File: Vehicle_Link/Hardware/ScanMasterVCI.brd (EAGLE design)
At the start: 53 x 39.4 mm, 88 parts, among them IC1 XMEGA32A4U, Q1 MMBT4403, Q10 ZXMP6A17G, Q2 MMBT3904, Q3 MMBT3904, Q4 MMBT3904, Q5 MMBT3904, Q6 MMBT3904, Q7 NTZD5110N, Q8 NTZD5110N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

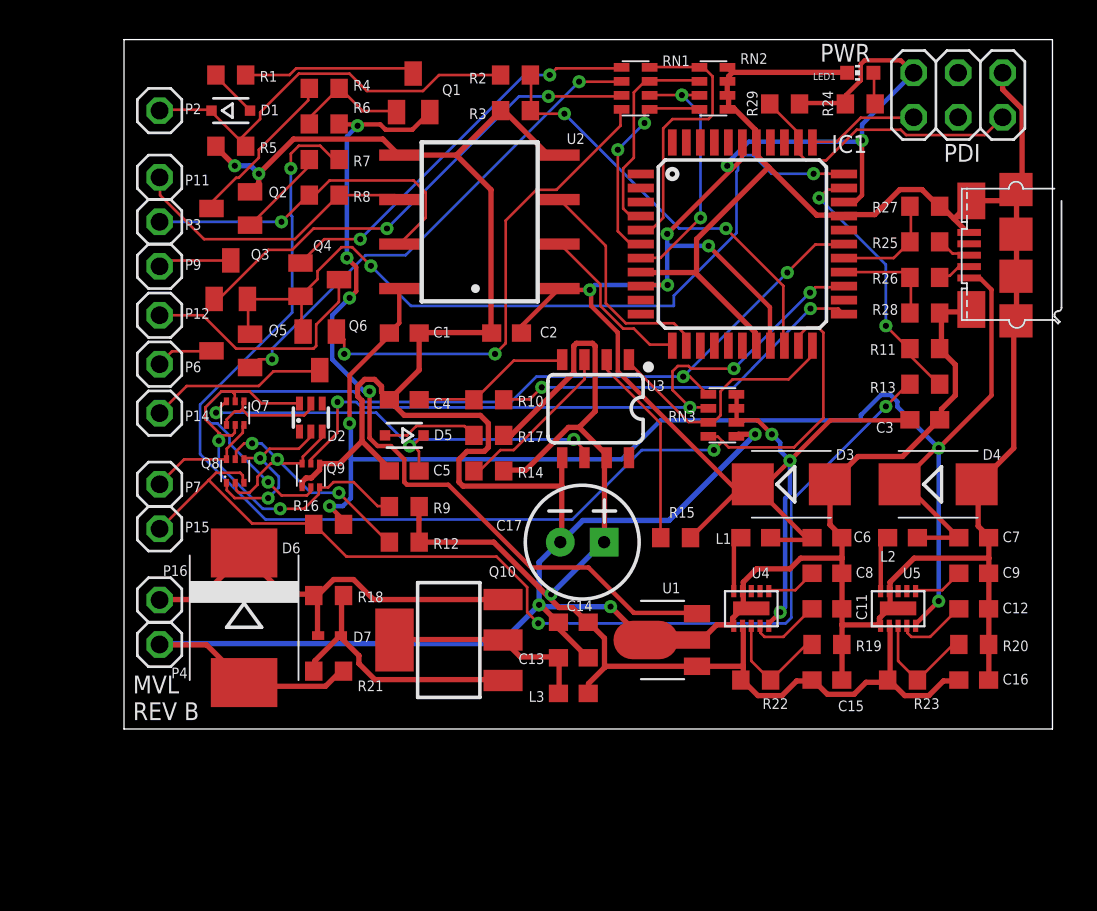
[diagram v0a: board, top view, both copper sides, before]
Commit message: Added LED. Fixed soldering issues. 8V IC pins were wrong.
Added an LED for comm indication. Added resistor for this LED. The L78L pinout had VIN and VOUT swapped somehow, fixed this. The MAX17502 has proven very difficult to solder, even with paste. The pad below the chip causes bridging in extreme cases so I fixed that as well.
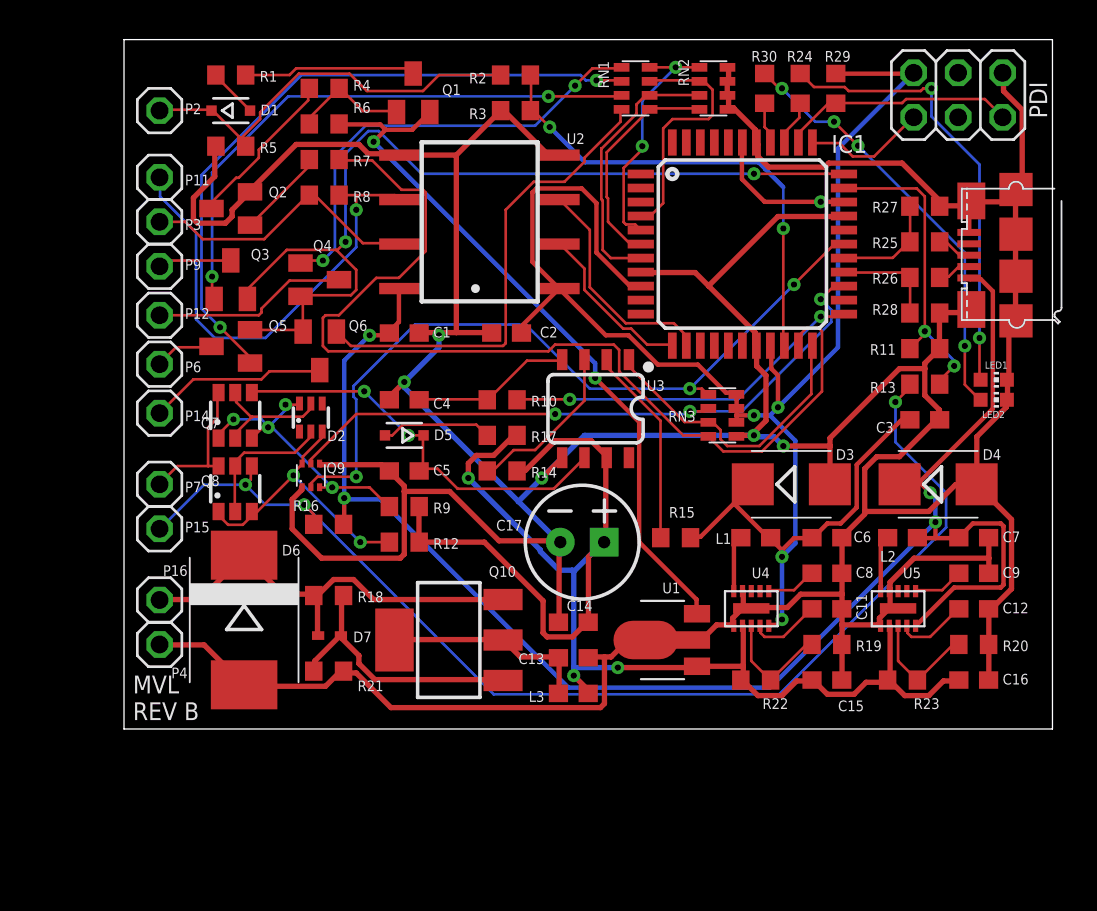
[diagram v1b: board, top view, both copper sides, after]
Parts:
- added LED2: RED, led:CHIP-LED0603
- added R30: 120, resistor:R0603
- Q7, Q8: value NTZD5110N -> NDC7002N; device customics:SOT563 -> customics:SSOT6
- moved LED1 19.1 mm to (49.7, 19.9), turned to 270 degrees
- moved R24 3.54 mm to (38.6, 36.6), turned to 270 degrees
- moved R29 3.05 mm to (40.6, 36.6), turned to 90 degrees
- moved Q8 1.02 mm to (6.35, 13.7)
- moved R10 0.76 mm to (21.6, 18.8)
- moved R14 0.76 mm to (21.6, 14.7)
- moved R17 0.76 mm to (21.6, 16.8)
- moved Q5 0.25 mm to (6.10, 21.8)
- moved D6 0.13 mm to (6.86, 6.22)
- moved Q7 0.13 mm to (6.35, 17.9), turned to 0 degrees
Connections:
- new net COM-LED: IC1.37, R30.2
- new net N$27: LED2.A, R30.1
- new net PWR-LED: IC1.36, R24.2
- net +3V3: no longer R24.2
- net GND: now also LED2.C
- net ISO-K: now also Q7.4; no longer Q7.3
- net J1962-15: now also Q8.4; no longer Q8.3
- net N$1: now also Q8.2, Q8.5; no longer Q8.1, Q8.4
- net N$11: now also Q7.1, Q7.3; no longer Q7.2, Q7.5
- net N$4: now also Q7.2, Q7.5; no longer Q7.1, Q7.4
- net N$5: now also Q8.1, Q8.3; no longer Q8.2, Q8.5
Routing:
- net GND: track 285.1 -> 310.7 mm
- net N$27: track 0.00 -> 24.5 mm, vias 0 -> 4
- net N$2: track 1.82 -> 25.8 mm, vias 0 -> 2
- net J1850VPW-TX: track 70.6 -> 57.2 mm, vias 2 -> 0
- net J1962-11: track 16.9 -> 27.2 mm, vias 0 -> 1
- net N$21: track 28.3 -> 38.4 mm
- net +8V: track 49.4 -> 41.3 mm, vias 4 -> 2
- net SCI-A-TX-EN: track 51.7 -> 43.8 mm
- net N$11: track 23.9 -> 16.9 mm, vias 2 -> 4
- net J1962-15: track 60.4 -> 67.2 mm, vias 2 -> 3
- net +12V: track 77.9 -> 84.5 mm, vias 1 -> 3
- net +5V: track 85.5 -> 91.3 mm
- net SCI-TX: track 48.1 -> 53.7 mm
- net N$22: track 28.1 -> 32.5 mm
- net J1962-3: track 20.0 -> 16.3 mm, vias 1 -> 0
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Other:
- board text removed: "PWR"

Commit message: Moved LED resistors next to LEDs because it made more sense
LED resistors were next to the XMEGA, moved them just so they'd be next to their respective LEDs, and because it would space out the LEDs more.
Forgot to mention before, but since the NDC7002N MOSFET is coming back into stock, I've switched two of my MOSFETs back to those, since that's how the original schematic had it.
Moved around part labels so they weren't overlapping vias.
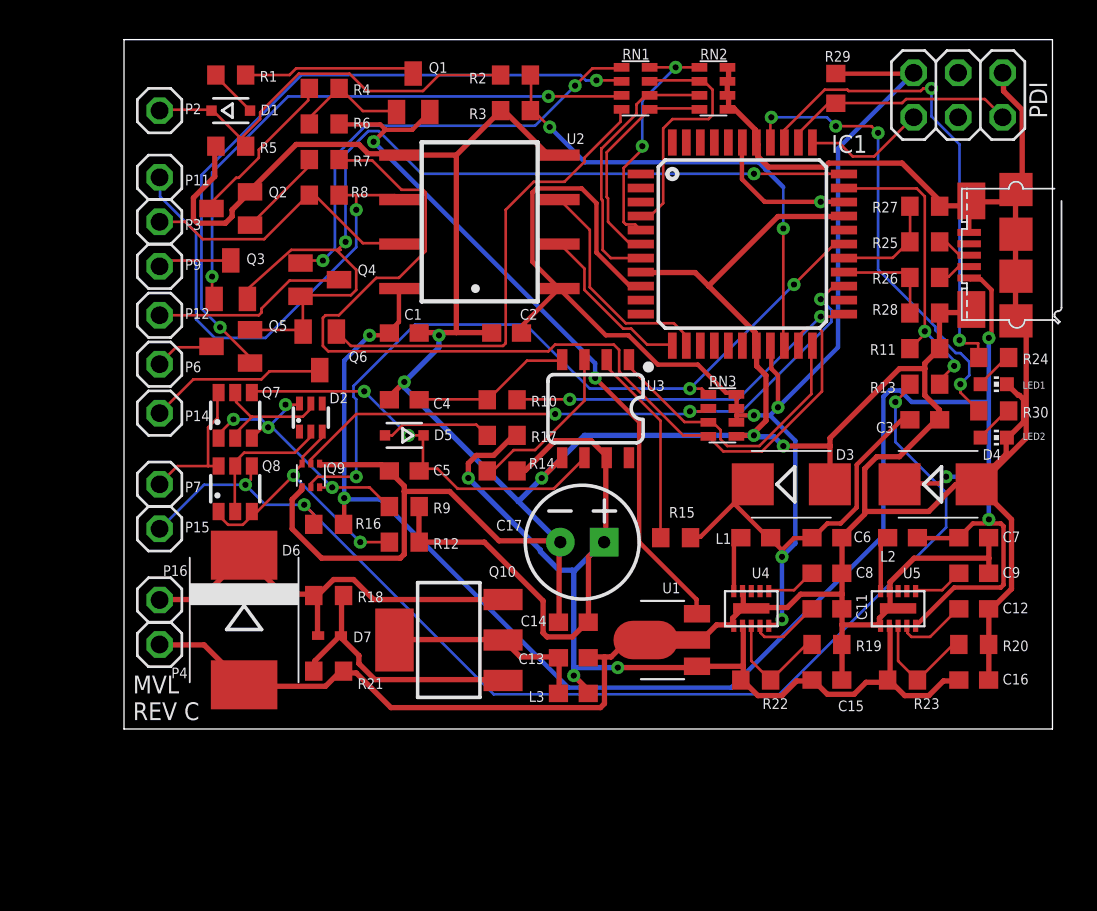
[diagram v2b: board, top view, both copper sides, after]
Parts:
- moved R30 22.6 mm to (49.7, 18.2), turned to 180 degrees
- moved R24 18.9 mm to (49.7, 21.2), turned to 180 degrees
- moved LED2 2.16 mm to (49.7, 16.6)
- moved LED1 0.25 mm to (49.7, 19.7)
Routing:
- net PWR-LED: track 2.61 -> 27.2 mm, vias 0 -> 2
- net COM-LED: track 2.37 -> 26.8 mm, vias 0 -> 4
- net N$2: track 25.8 -> 2.29 mm, vias 2 -> 0
- net N$27: track 24.5 -> 2.29 mm, vias 4 -> 0
- net +5V: track 91.3 -> 103.6 mm, vias 4 -> 5
- net GND: track 310.7 -> 318.6 mm
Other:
- board text added: "MVL REV C"
- board text removed: "MVL REV B"

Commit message: Scrubbed ISO1050 from board, replaced with MAX13444EASA+
Using the CAN tranceiver was not working with CCD, so I've gone with an RS-485 IC instead. I've tested this IC with CCD and can confirm it works for reading.
Started the process of removing the device names from the board view, instead I will be showing the values for resistors, capacitors, and inductors, for ease of assembly.
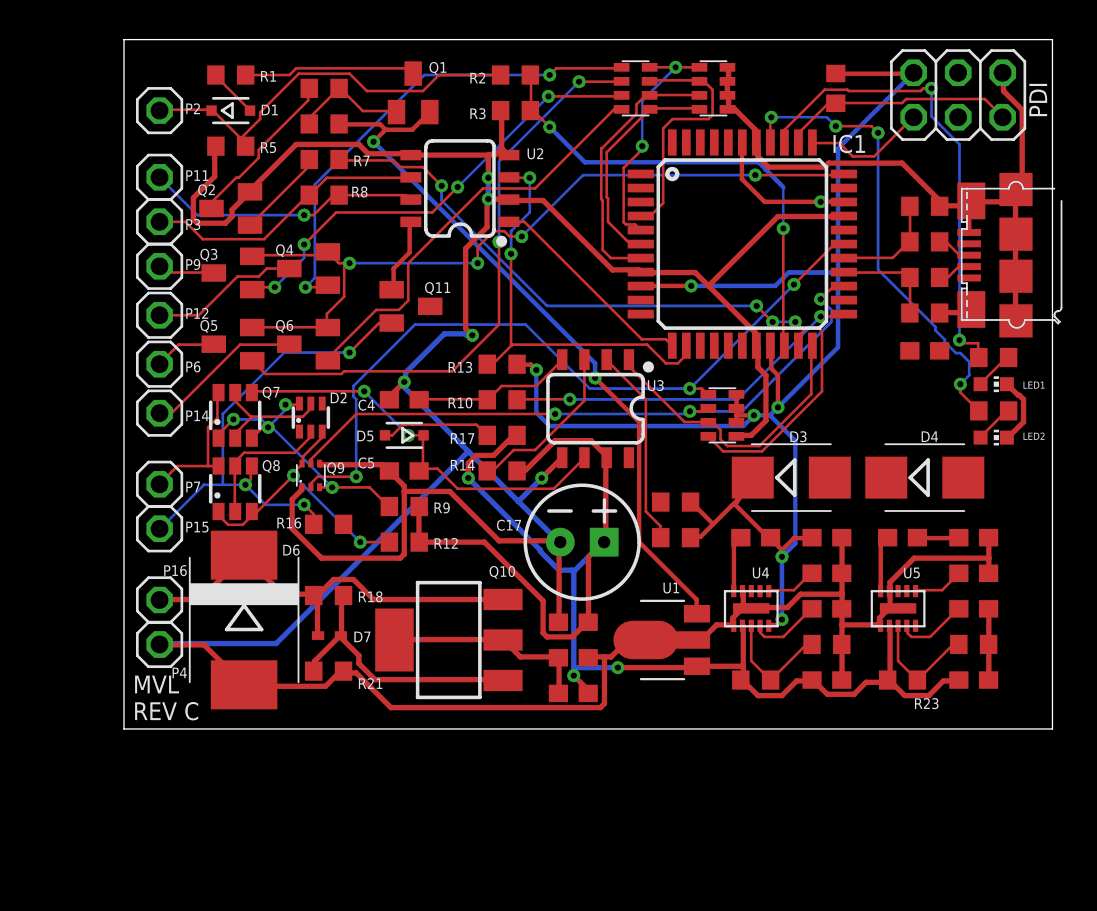
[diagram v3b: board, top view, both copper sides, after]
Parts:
- removed C1, C2: 0.1uF, adafruit:C0603
- added Q11: MMBT3904, semicon-smd-ipc:SOT23
- C8, C9: value 3300pF -> 3.3nF
- R11: value 1910 -> 1k
- RN1: value 742C083104JP -> 1k
- RN2: value 742C083104JP -> 100k
- RN3: value 742C083104JP -> 1K
- U2: value ISO1050 -> MAX13444EASA+; device customics:SOP08 -> customics:SO08
- moved R13 24.2 mm to (21.6, 20.8), turned to 0 degrees
- moved R11 16.7 mm to (31.5, 13.0), turned to 0 degrees
- moved C3 3.94 mm to (45.7, 21.6)
- moved U2 2.01 mm to (19.2, 30.9)
- moved Q4 0.90 mm to (10.5, 26.3), turned to 90 degrees
- moved D4 0.85 mm to (45.7, 14.4)
- moved Q6 0.74 mm to (10.5, 22.0), turned to 90 degrees
- moved Q3 0.40 mm to (6.22, 26.0), turned to 90 degrees
- moved D3 0.38 mm to (38.1, 14.4)
- moved Q5 0.18 mm to (6.22, 22.0)
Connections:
- net +3V3: now also R11.2, R13.2; no longer C2.1, U2.1
- net +5V: now also Q11.1; no longer C1.1
- net CCD-RX: now also U2.1; no longer U2.2
- net CCD-TX: now also R13.1
- net GND: now also U2.2; no longer C1.2, C2.2, R11.1
- net J1962-11: now also U2.7; no longer U2.6
- net J1962-15: now also Q11.2; no longer R13.2
- net J1962-3: now also U2.6; no longer U2.7
- net SCI-RX: now also Q11.3, R11.1; no longer R11.2, R13.1
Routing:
- net +5V: track 103.6 -> 6.76 mm, vias 5 -> 0
- net GND: track 318.6 -> 273.1 mm
- net J1962-15: track 67.2 -> 28.2 mm
- net SCI-RX: track 17.9 -> 0.00 mm, vias 2 -> 0
- net J1850VPW-TX: track 57.2 -> 45.0 mm, vias 0 -> 4
- net +3V3: track 112.3 -> 100.9 mm, vias 5 -> 7
- net J1962-11: track 27.2 -> 15.8 mm
- net CCD-TX: track 13.0 -> 24.2 mm, vias 0 -> 2
- net SCI-TX: track 54.1 -> 45.5 mm, vias 2 -> 4
- net N$22: track 32.5 -> 26.1 mm, vias 2 -> 4
- net N$21: track 38.4 -> 33.8 mm
- net N$23: track 27.2 -> 24.0 mm
- net J1962-12: track 11.2 -> 8.51 mm
- net CCD-RX: track 9.57 -> 12.3 mm
- net N$13: track 26.0 -> 27.7 mm
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
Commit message: Finished replacing names with values on the board view. Resistors, capacitors and inductors all should be showing the values instead of the names on the board view. This makes organizing parts for assembly much easier.
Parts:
- RN3: value 1K -> 100k
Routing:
- net +5V: track 6.76 -> 22.0 mm, vias 0 -> 2

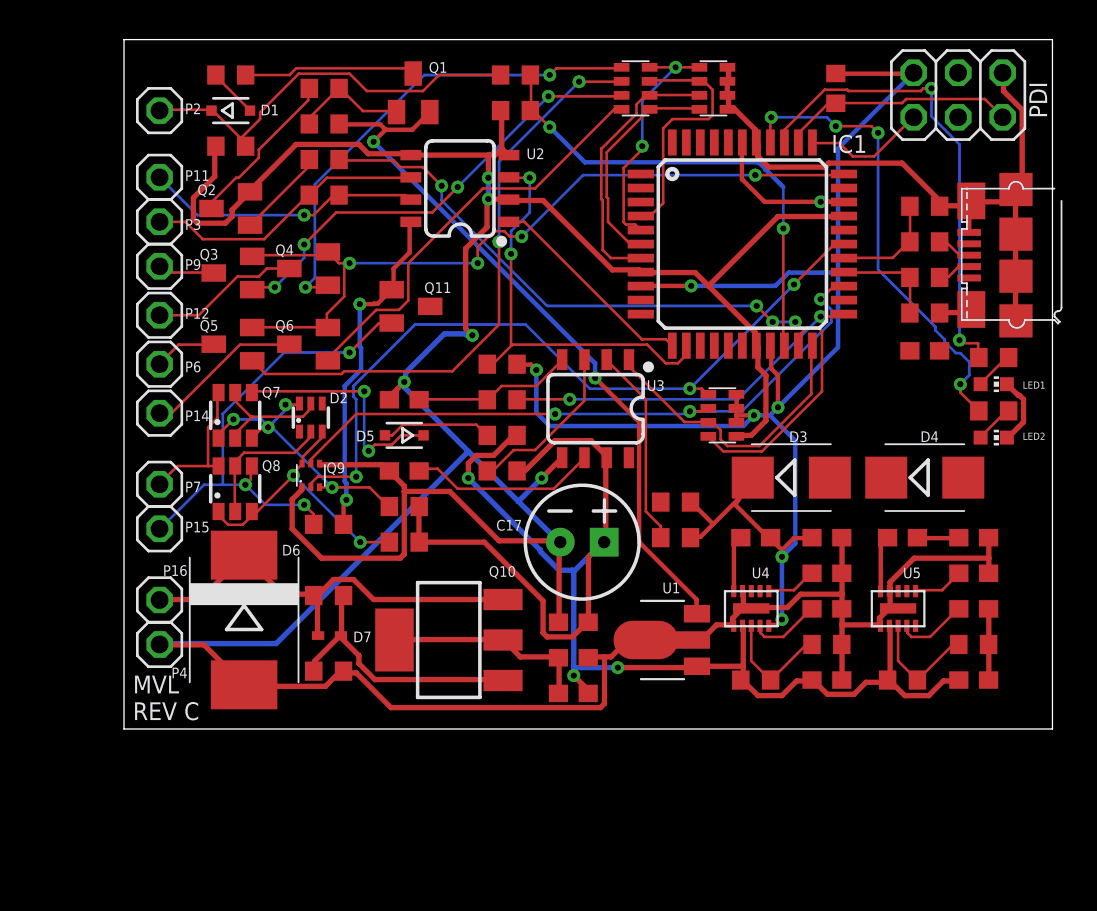
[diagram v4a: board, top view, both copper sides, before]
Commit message: Cleared up the last few airwires.
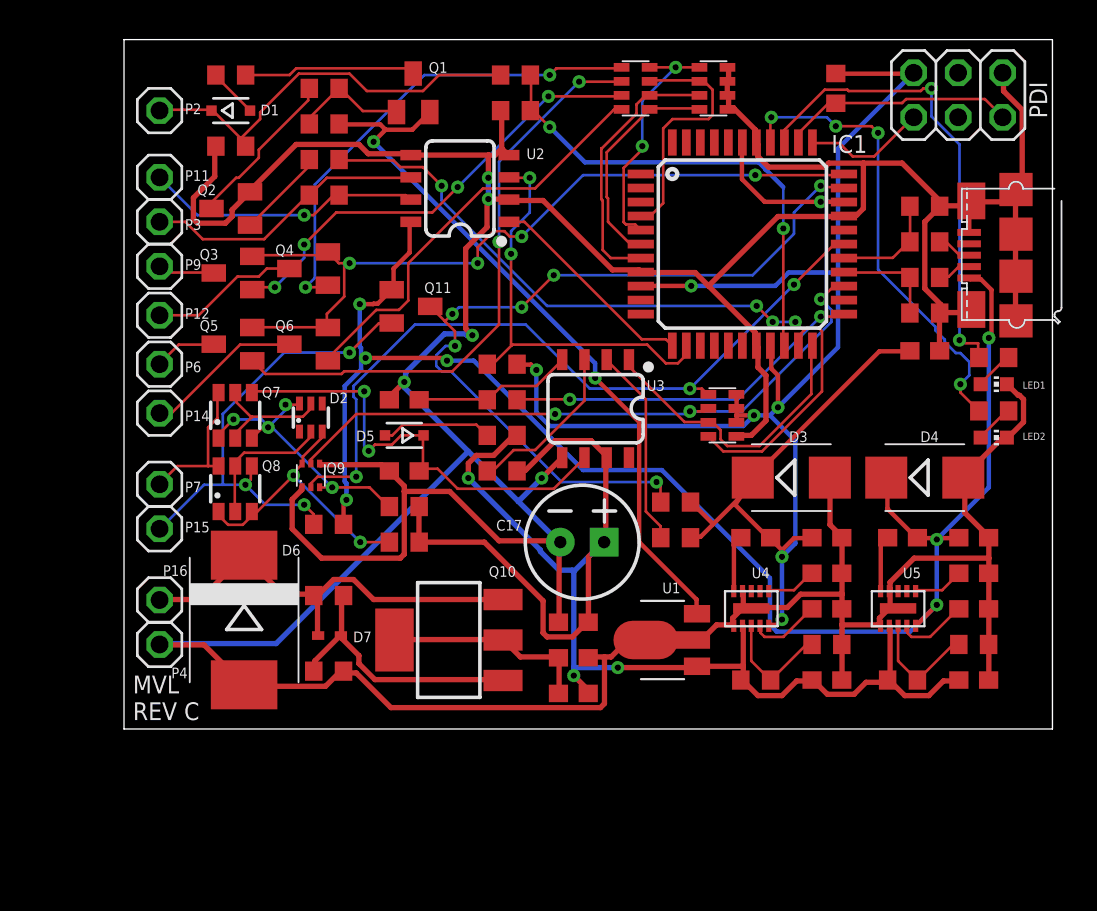
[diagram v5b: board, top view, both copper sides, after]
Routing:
- net +5V: track 22.0 -> 90.4 mm, vias 2 -> 7
- net SCI-RX: track 0.00 -> 48.1 mm, vias 0 -> 6
- net GND: track 273.1 -> 299.2 mm
- net +3V3: track 100.9 -> 112.8 mm
- net ISO-K: track 24.2 -> 26.3 mm

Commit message: Corrected the 8V IC being the wrong way around. Fixed pull-up resistors.
Lots of pull-up resistors were 10k, or even 100k, and that doesn't really seem to work in practical cases, so I've corrected them all to be 1k. For CCD, since I had 3 1K resistors close to each other I've replaced them with a single resistor array.
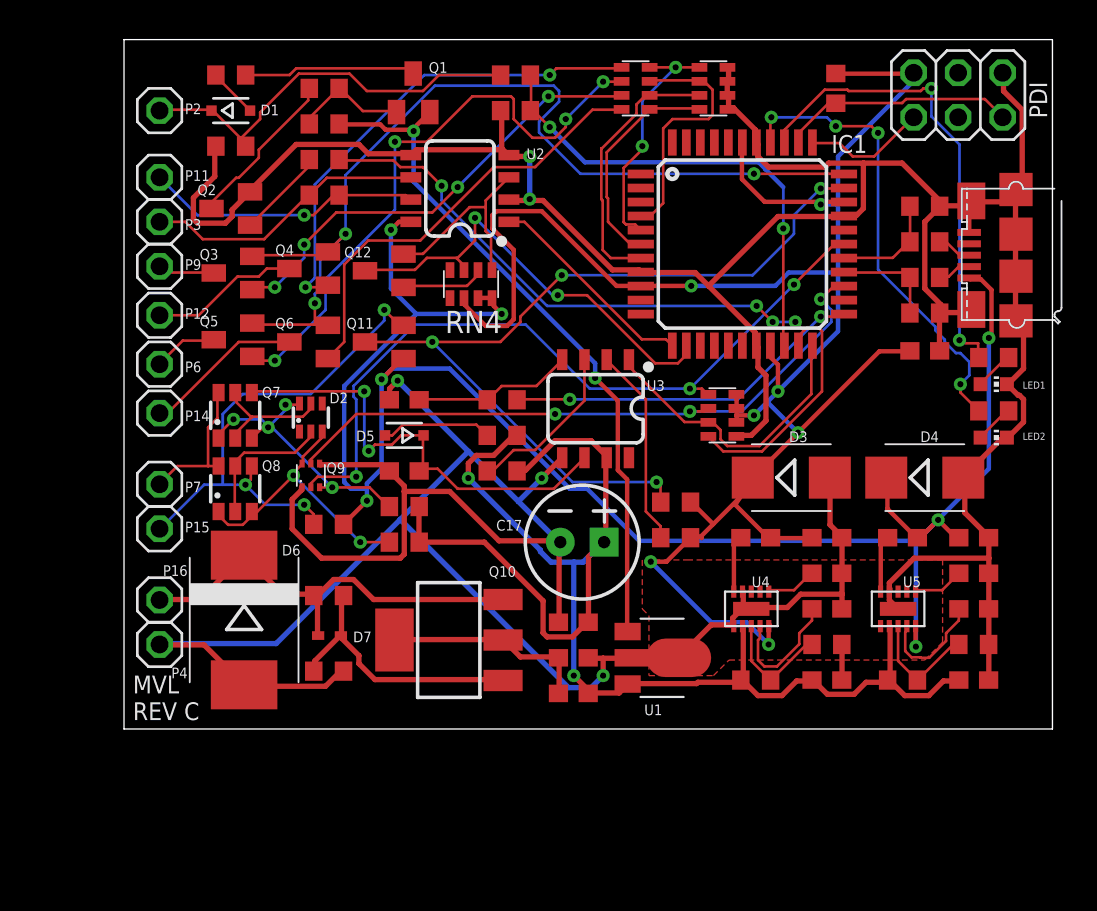
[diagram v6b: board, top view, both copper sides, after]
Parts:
- removed R13: 1k, adafruit:R0603
- added Q12: MMBT3904, semicon-smd-ipc:SOT23
- added RN4: 1k, resistor-net:CTS742C083
- R14: value 10k -> 1k
- R15: value 100k -> 1k
- moved Q11 2.54 mm to (14.9, 22.1), turned to 90 degrees
- moved U1 1.02 mm to (30.7, 4.06), turned to 270 degrees
- moved U4 0.51 mm to (35.8, 6.86)
- moved U5 0.51 mm to (44.2, 6.86)
- moved Q5 0.25 mm to (6.22, 22.2)
- moved Q6 0.13 mm to (10.5, 22.1)
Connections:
- new net N$32: Q12.2, RN4.1, U2.3
- new net N$33: Q12.1, RN4.2
- net +12V: now also U1.3; no longer U1.1
- net +3V3: now also RN4.6; no longer R13.2
- net +5V: now also RN4.7, RN4.8
- net +8V: now also U1.1; no longer U1.3
- net CCD-TX: now also Q12.3, RN4.3; no longer R13.1, U2.3
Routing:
- net GND: track 299.2 -> 282.1 mm
- net +5V: track 90.4 -> 104.4 mm
- net N$32: track 0.00 -> 11.8 mm
- net SCI-TX: track 45.5 -> 55.1 mm, vias 4 -> 3
- net N$33: track 0.00 -> 4.81 mm
- net +3V3: track 112.8 -> 116.3 mm
- net N$9: track 4.11 -> 7.33 mm
- net N$15: track 4.11 -> 6.48 mm
- net +8V: track 41.3 -> 39.5 mm
- net J1962-15: track 28.2 -> 29.9 mm
- net N$23: track 24.0 -> 25.3 mm
- net CCD-TX: track 24.2 -> 25.4 mm
- net SCI-RX: track 48.1 -> 49.2 mm, vias 6 -> 4
- net +12V: track 84.5 -> 83.9 mm, vias 3 -> 2
- net N$21: track 33.8 -> 34.0 mm, vias 2 -> 4
- added copper zone on layer 1, net GND
